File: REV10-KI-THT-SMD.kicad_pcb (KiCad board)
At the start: 2 copper layers, 114.3 x 73 mm, 44 parts, among them J1 EJ508A (PWR), J2 54-00298, P1 SPADE, P2 SPADE, Q1 2N3904, U1 NJM78M05FA, U2 LMC555CN, U3 STQ1HNK60R-AP, U4 STQ1HNK60R-AP, U5 TL5001AIP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

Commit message: first dual
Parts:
- C8: footprint THT-SMD:C_THT_SMD -> THT-SMD:CHV
- moved Q1 21.6 mm to (109.7, 75.9)
- moved R1 16.4 mm to (98.8, 90.5), turned to 0 degrees
- moved C5 8.17 mm to (122.3, 85.1), turned to -90 degrees
- moved C8 6.74 mm to (195.8, 75.1)
- moved R5 6.58 mm to (99.0, 77.9)
- moved D2 5.38 mm to (187.7, 75.1)
- moved U3 5.32 mm to (163.1, 76.5)
- moved U4 5.23 mm to (170.9, 76.5)
- moved U1 5.20 mm to (110.9, 95.5), turned to -90 degrees
- moved R3 5.09 mm to (98.9, 87.1)
- moved C7 4.87 mm to (142.6, 82.6)
- moved C6 4.71 mm to (166.5, 89.6), turned to 180 degrees
- moved R13 4.69 mm to (188.7, 78.7)
- moved C2 4.32 mm to (98.9, 74.8)
- moved C3 3.78 mm to (104.3, 98.6), turned to 90 degrees
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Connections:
- U6 pad P$10: GND -> unconnected-(U6-PadP$10)
- U6 pad P$16: GND -> unconnected-(U6-PadP$16)
- U6 pad P$17: FINAL_SIGNAL -> unconnected-(U6-PadP$17)
- U6 pad P$26: unconnected-(U6-PadP$26) -> GND
- U6 pad P$6: unconnected-(U6-PadP$6) -> FINAL_SIGNAL
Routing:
- net Net-(D1-A): track 19.2 -> 69.8 mm
- net Net-(C2-Pad1): track 6.86 -> 53.1 mm
- net +5V: track 102.6 -> 139.1 mm
- net Net-(D2-K): track 0.00 -> 31.5 mm
- net Net-(U2-DIS): track 2.54 -> 29.4 mm
- net GND: track 0.00 -> 26.2 mm
- net Net-(Q1-C): track 0.00 -> 20.0 mm
- net +9V: track 0.00 -> 19.5 mm
- net Net-(Q1-B): track 0.00 -> 18.5 mm
- net FINAL_SIGNAL: track 105.9 -> 124.0 mm
- net Net-(J2-Pad1): track 0.00 -> 17.5 mm
- net Net-(U5-FB): track 20.3 -> 37.2 mm
- net Net-(FH2-Pad1): track 6.86 -> 22.3 mm
- net BATT+: track 29.1 -> 44.1 mm
- net Net-(U5-SCP): track 16.3 -> 7.42 mm
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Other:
- board text added: "REV-10"
- board text removed: "400V!!!"
- board text removed: "DO NOT PUT IN BACKWARDS"
- board text removed: "R9THT"

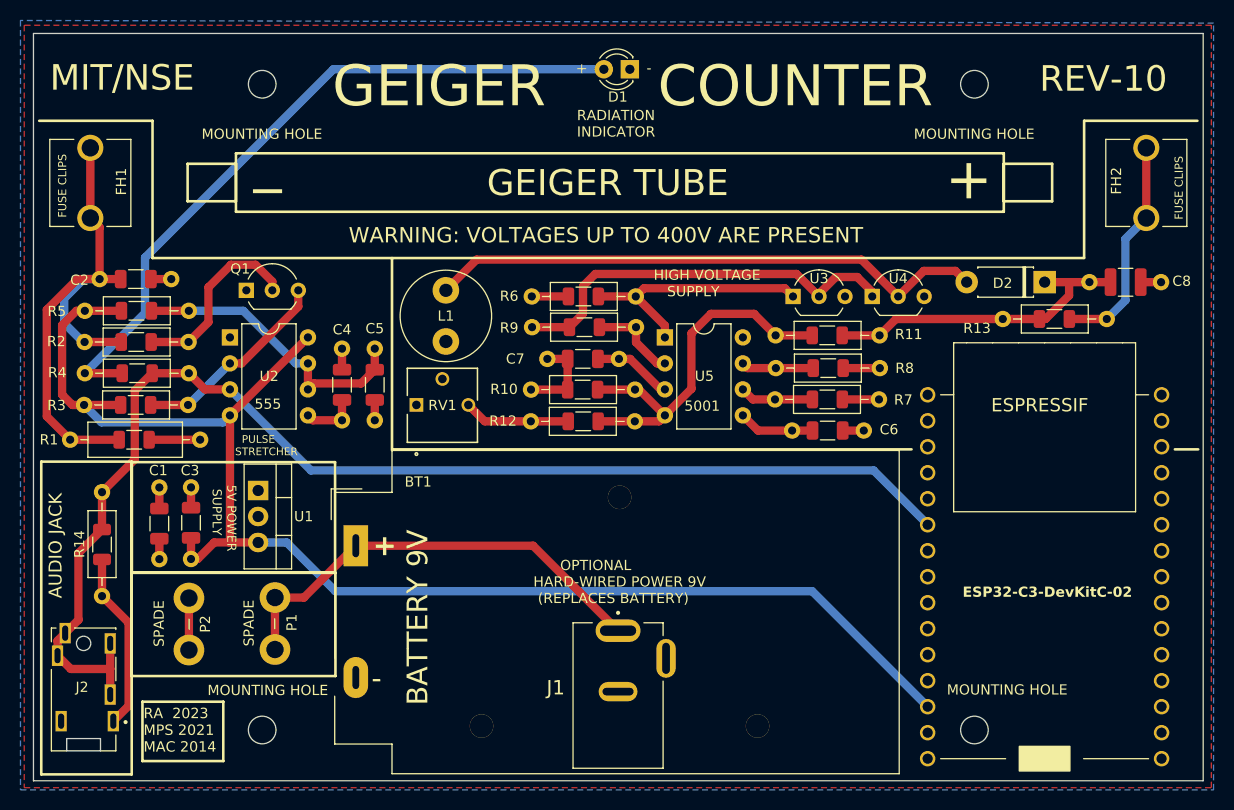
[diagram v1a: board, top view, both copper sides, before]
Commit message: added holes for m4011, removed rev 9 backups
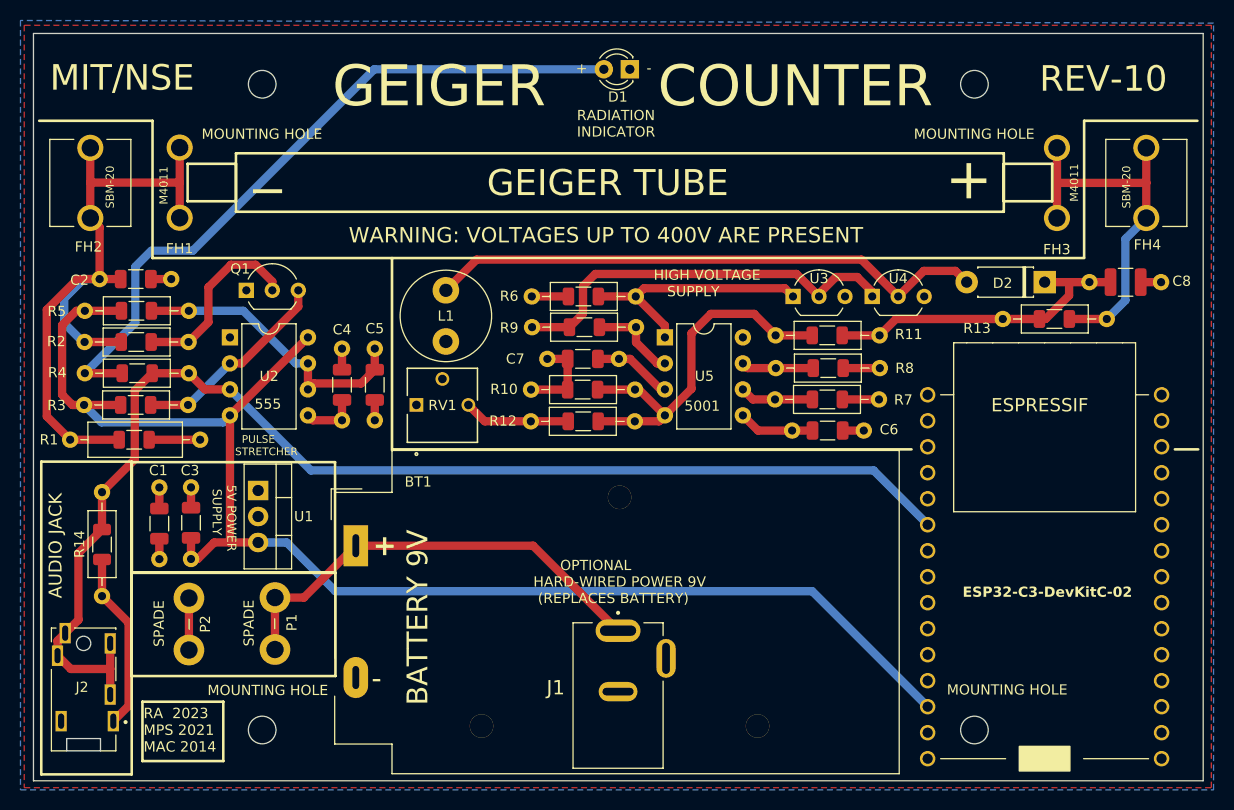
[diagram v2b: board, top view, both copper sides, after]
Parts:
- added FH1: ~, 36-3530-ND:36-3530-ND, F.Cu at (103.2, 65.4)
- added FH3: ~, 36-3530-ND:36-3530-ND, F.Cu at (188.9, 65.4)
- renumbered FH1 to FH2, FH2 to FH4
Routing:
- net Net-(C2-Pad1): track 53.1 -> 68.7 mm
- net Net-(FH3-Pad1): track 22.3 -> 37.9 mm
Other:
- board text added: "M4011"
- board text added: "SBM-20"
- board text removed: "FUSE CLIPS"

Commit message: added readme
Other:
- board text added: "RA 2023 MPS 2021 MAC 2014 MDA 2014"
- board text removed: "RA 2023 MPS 2021 MAC 2014"
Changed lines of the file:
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@@
 			)
 			(layer "F.CrtYd")
-			(net 221383328)
 		)
 		(fp_line
@@
 			)
 			(layer "F.CrtYd")
-			(net 221383328)
 		)
 		(fp_line
@@
 	(gr_rect
 		(start 99.55 116.1)
-		(end 107.45 121.9)
+		(end 107.45 123.075)
 		(stroke
 			(width 0.254)
@@
 		)
 	)
-	(gr_text "RA  2023\nMPS 2021\nMAC 2014"
-		(at 99.65 121.1 0)
-		(layer "F.SilkS")
-		(effects
+	(gr_text "RA  2023\nMPS 2021\nMAC 2014\nMDA 2014"
+		(at 99.625 122.7 0)
+		(layer "F.SilkS")
+		(effects
